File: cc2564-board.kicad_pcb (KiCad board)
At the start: 2 copper layers, 70 parts, among them J1 TYPE-C-31-M-12, J2 Conn_ARM_JTAG_SWD_10, J3 Conn_01x16, J4 Conn_01x16, J5 BOOT1, J6 BOOT0, J7 1909763-1, J8 Conn_01x04, SW1 SW_Push, U1 LD1117#33, U2 USBLC6-2P6, U3 LD1117#18, U4 STM32F103C8Tx, U5 TXB0104D, U6 TXB0104D, U7 CC2564CRVMR, Y1 ECS-80-18-30-JGN-TR, Y2 ECS-327MVATX-3-CN-TR, Y3 ECS-260-8-36CKM-TR

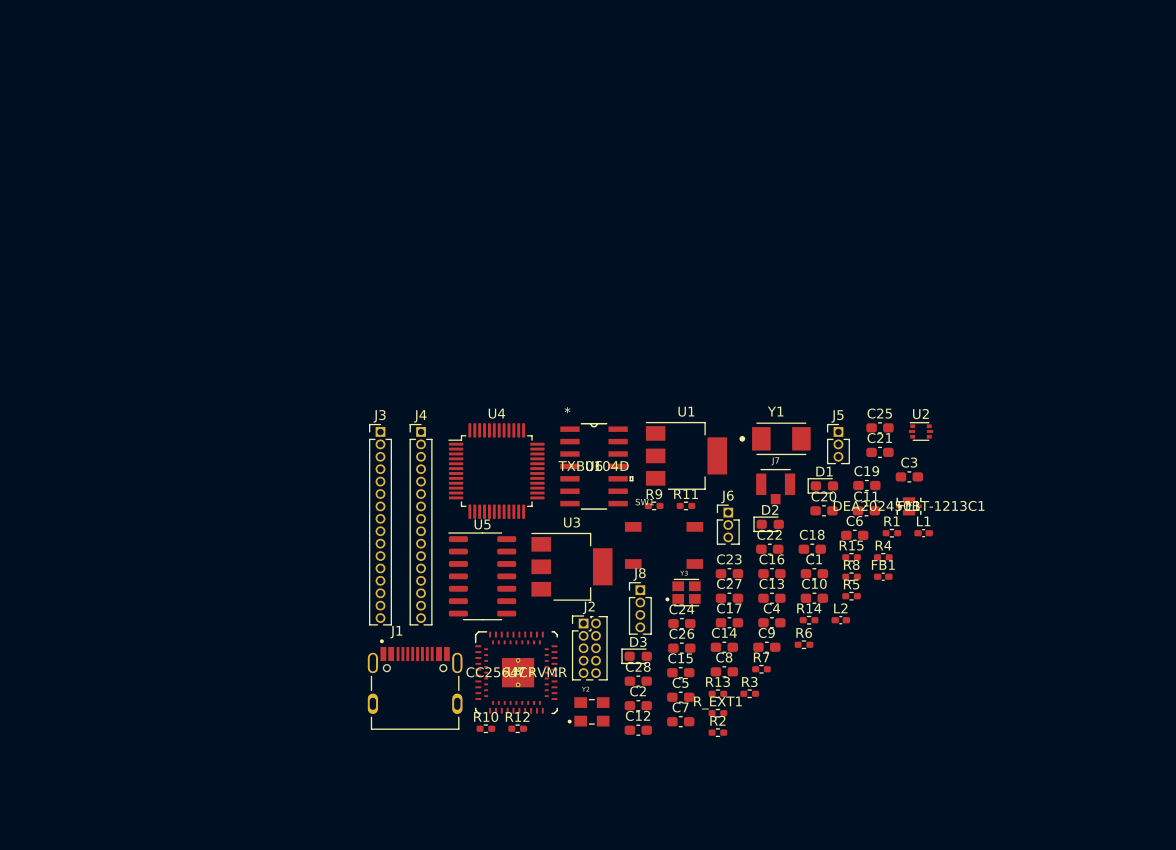
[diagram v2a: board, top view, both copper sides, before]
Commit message: One header for boot mode
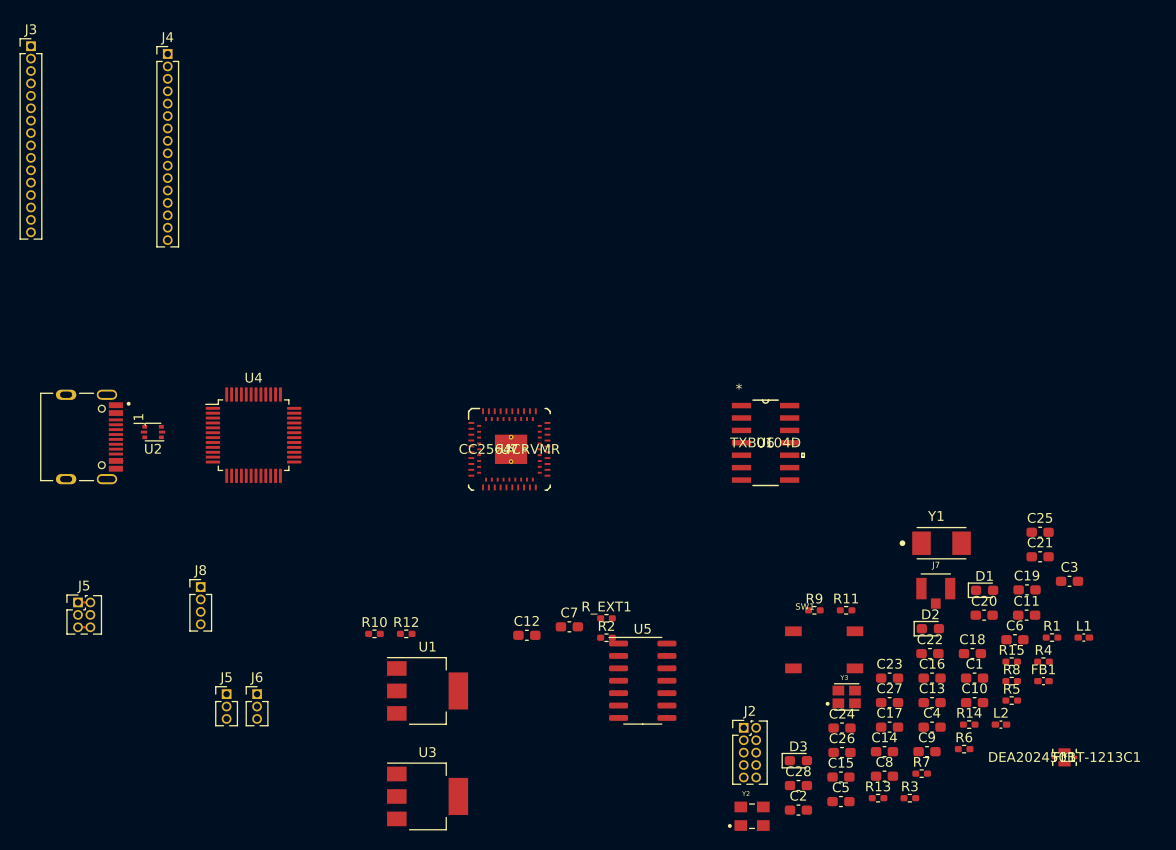
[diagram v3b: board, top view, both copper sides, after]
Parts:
- added J5: BOOT, Connector_PinHeader_1.27mm:PinHeader_2x03_P1.27mm_Vertical, F.Cu at (73.4, 81.7)
- moved U2 78.6 mm to (81.1, 64.3), turned to 180 degrees
- moved J5 68.1 mm to (88.6, 91.1)
- moved J3 53.3 mm to (68.6, 24.8)
- moved J6 51.7 mm to (91.7, 91.1)
- moved J4 46.6 mm to (82.6, 25.6)
- moved J8 45.0 mm to (86.0, 80.2)
- moved J1 45.0 mm to (72.2, 64.8), turned to 270 degrees
- moved U1 35.8 mm to (109.2, 90.8)
- moved FL1 30.2 mm to (174.4, 97.6)
- moved U3 27.8 mm to (109.2, 101.6)
- moved U4 25.2 mm to (91.4, 64.6)
- moved U7 22.9 mm to (117.6, 66.1)
- moved C11 19.6 mm to (170.5, 83.0)
- moved C13 19.6 mm to (160.8, 92.0)
- moved C15 19.6 mm to (151.5, 99.6)
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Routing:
- net VDD_3V3: track 0.00 -> 1.27 mm
- net GND: track 0.00 -> 1.27 mm
- net VCC_USB: track 0.00 -> 0.67 mm
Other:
- copper layers 2 -> 4

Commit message: Use meandered PIFA from TI app note AN043
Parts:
- added AE1: TI SWRA117D meandered IFA, RF_Antenna:Texas_SWRA117D_2.4GHz_Right, F.Cu at (213.6, 93.3)

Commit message: More footprint updates
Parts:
- C1, C10, C11, C12, C13, C14, C15, C16, C17, C18, C19, C2, C20, C21, C22, C23, C24, C25, C26, C27, C28, C3, C4, C5, C6, C7, C8, C9: footprint Capacitor_SMD:C_0603_1608Metric_Pad1.08x0.95mm_HandSolder -> Capacitor_SMD:C_0402_1005Metric_Pad0.74x0.62mm_HandSolder
- J5: value BOOT1 -> BOOT; footprint Connector_PinHeader_1.27mm:PinHeader_1x03_P1.27mm_Vertical -> Connector_PinHeader_1.27mm:PinHeader_2x03_P1.27mm_Vertical
- moved AE1 76.3 mm to (163.1, 36.1), turned to 270 degrees
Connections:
- J5 pad 2: BOOT1 -> VDD_3V3
- J5 pad 3: GND -> BOOT1

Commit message: Switch to nightly, initial board setup, not exactly sure what to git add...
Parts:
- removed the J5 at (88.6, 91.1)
- removed the J5 at (73.4, 81.7)
- removed J8: Conn_01x04, Connector_PinHeader_1.27mm:PinHeader_1x04_P1.27mm_Vertical
- removed Y3: ECS-260-8-36CKM-TR, cc2654-board-footprints:XTAL_ECS-160-10-36-JGN-TR
- added J5: BOOT, Connector_PinHeader_1.27mm:PinHeader_2x03_P1.27mm_Vertical, F.Cu at (134.2, 98.6)
- added R16: 10k, Resistor_SMD:R_0402_1005Metric_Pad0.72x0.64mm_HandSolder, F.Cu at (181.5, 101.7)
- added R17: 0, Resistor_SMD:R_0402_1005Metric_Pad0.72x0.64mm_HandSolder, F.Cu at (187.1, 97.8)
- C1, C11, C13, C3, C4, C5, C6, C8: value 100nF -> 0.1uF
- J6: value BOOT0 -> 1909763-1; footprint Connector_PinHeader_1.27mm:PinHeader_1x03_P1.27mm_Vertical -> cc2654-board-footprints:UFL-TE_1909763-1
- J7: value 1909763-1 -> Conn_01x04; footprint cc2654-board-footprints:UFL-TE_1909763-1 -> Connector_PinHeader_1.27mm:PinHeader_1x04_P1.27mm_Vertical
- R10: value 0 -> 10k
- R11: value 0 -> 1.5k
- R14: value 10k -> 0
- R4: value 90 -> 10k
- R5: value 55 -> 90
- R6: value 4 -> 55
- R7: value 10k -> 4
- R9: value 1.5k -> 10k
- moved J4 154.9 mm to (201.4, 125.0), turned to 180 degrees
- moved J1 140.9 mm to (190.6, 141.3), turned to 0 degrees
- moved J3 138.7 mm to (180.0, 107.4)
- moved U4 110.3 mm to (190.6, 112.8), turned to 90 degrees
- moved J6 108.3 mm to (199.9, 84.9), turned to -90 degrees
- moved U3 89.7 mm to (194.7, 128.8), turned to 90 degrees
- moved U1 85.9 mm to (186.2, 128.8), turned to 90 degrees
- moved U7 83.9 mm to (195.4, 97.3), turned to -90 degrees
- moved U2 75.1 mm to (153.5, 84.4), turned to 0 degrees
- moved Y1 53.5 mm to (190.5, 120.8), turned to 180 degrees
- moved AE1 53.0 mm to (191.0, 81.1), turned to 0 degrees
- moved L1 52.8 mm to (130.3, 111.2)
- moved R10 48.5 mm to (152.0, 89.6)
- moved C19 48.5 mm to (133.6, 111.8)
- moved SW1 46.4 mm to (110.1, 110.6)
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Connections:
- net Net-(J1-PadA8) renamed no_connect_77
- net Net-(J1-PadB8) renamed no_connect_78
- net Net-(J2-Pad8) renamed no_connect_79
- net Net-(U4-Pad2) renamed no_connect_80
- net Net-(U4-Pad3) renamed no_connect_81
- net Net-(U4-Pad4) renamed no_connect_82
- net Net-(U5-Pad10) renamed no_connect_83
- net Net-(U5-Pad11) renamed no_connect_84
- net Net-(U5-Pad12) renamed no_connect_85
- net Net-(U5-Pad3) renamed no_connect_86
- net Net-(U5-Pad4) renamed no_connect_87
- net Net-(U5-Pad5) renamed no_connect_88
- net Net-(U7-PadA1) renamed no_connect_89
- net Net-(U7-PadA12) renamed no_connect_90
- net Net-(U7-PadA13) renamed no_connect_91
- net Net-(U7-PadA14) renamed no_connect_92
- net Net-(U7-PadA15) renamed no_connect_93
- net Net-(U7-PadA16) renamed no_connect_94
- net Net-(U7-PadA18) renamed no_connect_95
- net Net-(U7-PadA19) renamed no_connect_96
- net Net-(U7-PadA20) renamed no_connect_97
- net Net-(U7-PadA21) renamed no_connect_98
- net Net-(U7-PadA22) renamed no_connect_99
- net Net-(U7-PadA23) renamed no_connect_100
- net Net-(U7-PadA27) renamed no_connect_101
- net Net-(U7-PadA30) renamed no_connect_102
- net Net-(U7-PadA31) renamed no_connect_103
- net Net-(U7-PadA35) renamed no_connect_104
- net Net-(U7-PadA36) renamed no_connect_105
- net Net-(U7-PadA37) renamed no_connect_106
- net Net-(U7-PadA39) renamed no_connect_107
- net Net-(U7-PadA40) renamed no_connect_108
- net Net-(U7-PadA7) renamed no_connect_109
- net Net-(U7-PadA8) renamed no_connect_110
- net Net-(U7-PadB1) renamed no_connect_111
- net Net-(U7-PadB10) renamed no_connect_112
- net Net-(U7-PadB12) renamed no_connect_113
- net Net-(U7-PadB13) renamed no_connect_114
- net Net-(U7-PadB14) renamed no_connect_115
- net Net-(U7-PadB16) renamed no_connect_116
- net Net-(U7-PadB17) renamed no_connect_117
- net Net-(U7-PadB20) renamed no_connect_118
- net Net-(U7-PadB23) renamed no_connect_119
- net Net-(U7-PadB28) renamed no_connect_120
- net Net-(U7-PadB29) renamed no_connect_121
- net Net-(U7-PadB30) renamed no_connect_122
- net Net-(U7-PadB31) renamed no_connect_123
- net Net-(U7-PadB32) renamed no_connect_124
- net Net-(U7-PadB33) renamed no_connect_125
- net Net-(U7-PadB34) renamed no_connect_126
- J2 pad 7: Net-(J2-Pad7) -> (no net)
- J6 pad 1: VDD_3V3 -> Net-(J6-Pad1)
- J6 pad 2: BOOT0 -> GND
- J7 pad 1: Net-(J7-Pad1) -> NSHUTDOWN_1V8
- J7 pad 2: GND -> BT_TX_DBG
- R10 pad 2: USB_D- -> BOOT1
- R11 pad 1: USB_D+ -> VDD_3V3
- R11 pad 2: Net-(R11-Pad2) -> USB_D+
- R12 pad 1: Net-(AE1-Pad1) -> Net-(R12-Pad1)
- R12 pad 2: Net-(C21-Pad1) -> USB_D-
- R13 pad 1: Net-(J7-Pad1) -> USB_D+
- R13 pad 2: Net-(C21-Pad1) -> Net-(R13-Pad2)
- R14 pad 1: VDD_1V8_32K -> Net-(AE1-Pad1)
- R14 pad 2: Net-(R14-Pad2) -> Net-(C21-Pad1)
- R15 pad 1: BT_SLOW_CLK -> Net-(J6-Pad1)
- R15 pad 2: Net-(R15-Pad2) -> Net-(C21-Pad1)
- R4 pad 1: VCC_USB -> Net-(R4-Pad1)
- R4 pad 2: Net-(D1-Pad2) -> BOOT0
- R5 pad 1: VDD_3V3 -> VCC_USB
- R5 pad 2: Net-(D2-Pad2) -> Net-(D1-Pad2)
- R6 pad 1: VDD_1V8 -> VDD_3V3
- R6 pad 2: Net-(D3-Pad2) -> Net-(D2-Pad2)
- R7 pad 1: VDD_3V3 -> VDD_1V8
- R7 pad 2: Net-(R7-Pad2) -> Net-(D3-Pad2)
- R9 pad 2: USB_D+ -> Net-(R9-Pad2)
- U4 pad 20: BOOT1 -> Net-(R10-Pad1)
- U4 pad 32: Net-(R10-Pad1) -> Net-(R12-Pad1)
- U4 pad 33: Net-(R11-Pad2) -> Net-(R13-Pad2)
- U4 pad 44: BOOT0 -> Net-(R4-Pad1)
- U5 pad 6: Net-(U5-Pad6) -> (no net)
- U5 pad 8: Net-(R7-Pad2) -> Net-(R8-Pad2)
- U5 pad 9: Net-(U5-Pad9) -> (no net)
- U6 pad 6: Net-(U6-Pad6) -> (no net)
- U6 pad 8: Net-(R8-Pad2) -> Net-(R9-Pad2)
- U6 pad 9: Net-(U6-Pad9) -> (no net)
- Y2 pad 1: Net-(R14-Pad2) -> Net-(R16-Pad2)
- Y2 pad 3: Net-(R15-Pad2) -> Net-(R17-Pad2)
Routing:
- net Net-(C22-Pad2): track 0.00 -> 3.68 mm
- net VDD_3V3: track 1.27 -> 0.00 mm
- net GND: track 1.27 -> 0.00 mm
- net VCC_USB: track 0.67 -> 0.00 mm
- added copper zone on In1.Cu, net GND
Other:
- board outline added: 25.9 x 67.9 mm
- net class Default removed

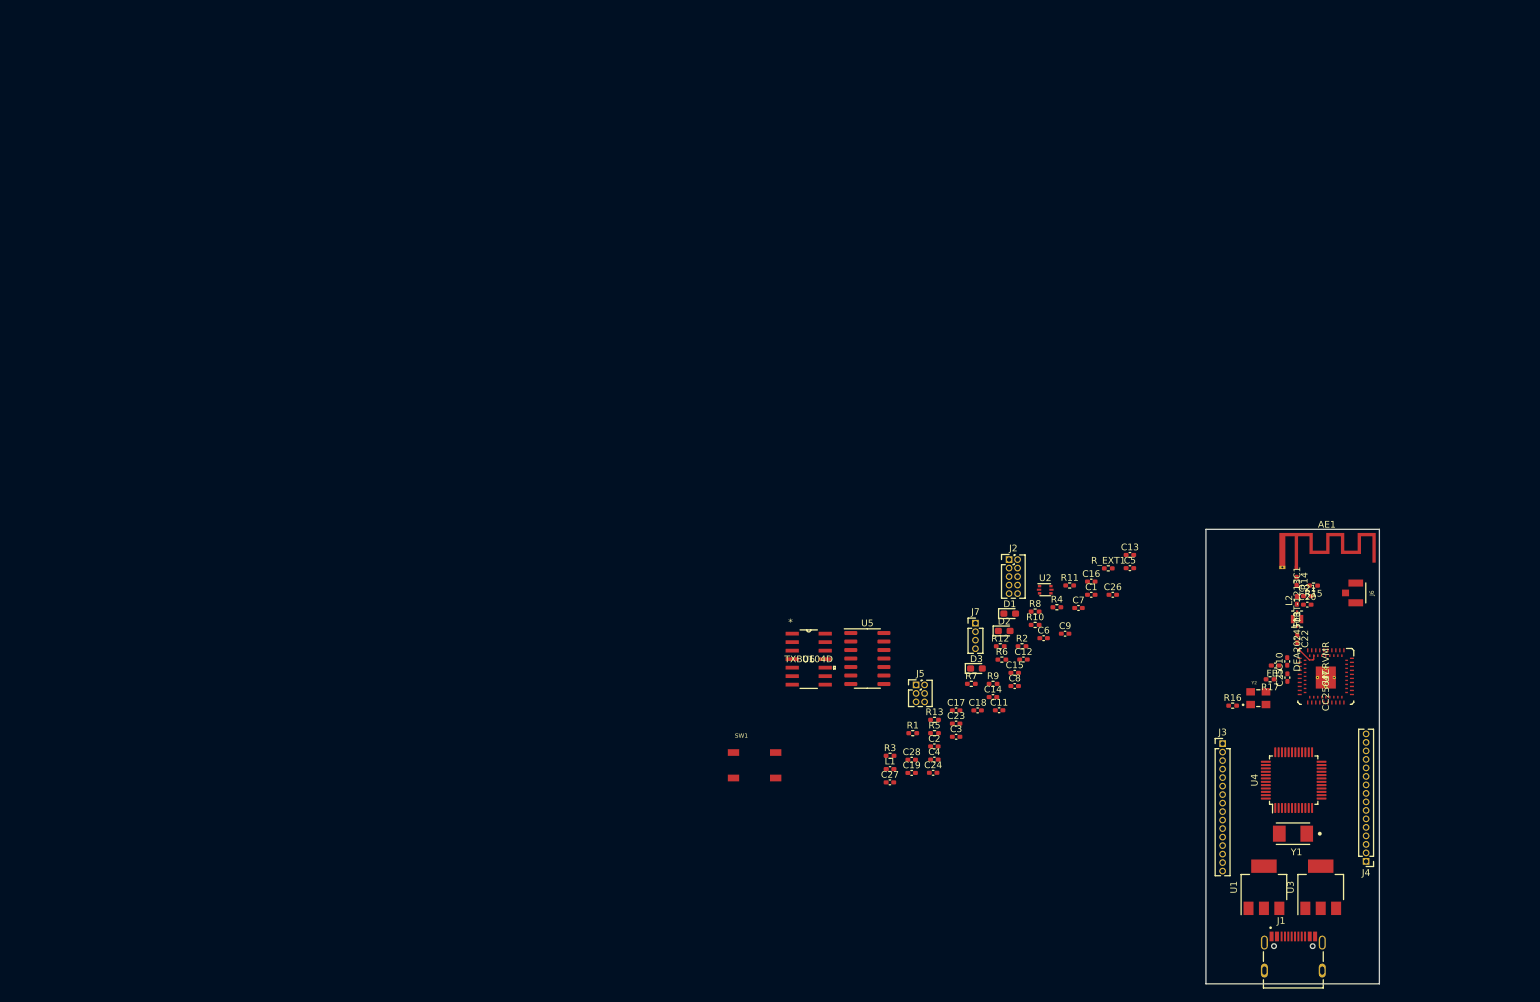
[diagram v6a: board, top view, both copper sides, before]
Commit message: Swap in TLV711 series 3v3/1v8 dual output LDO
Thanks @noahp for inspiration
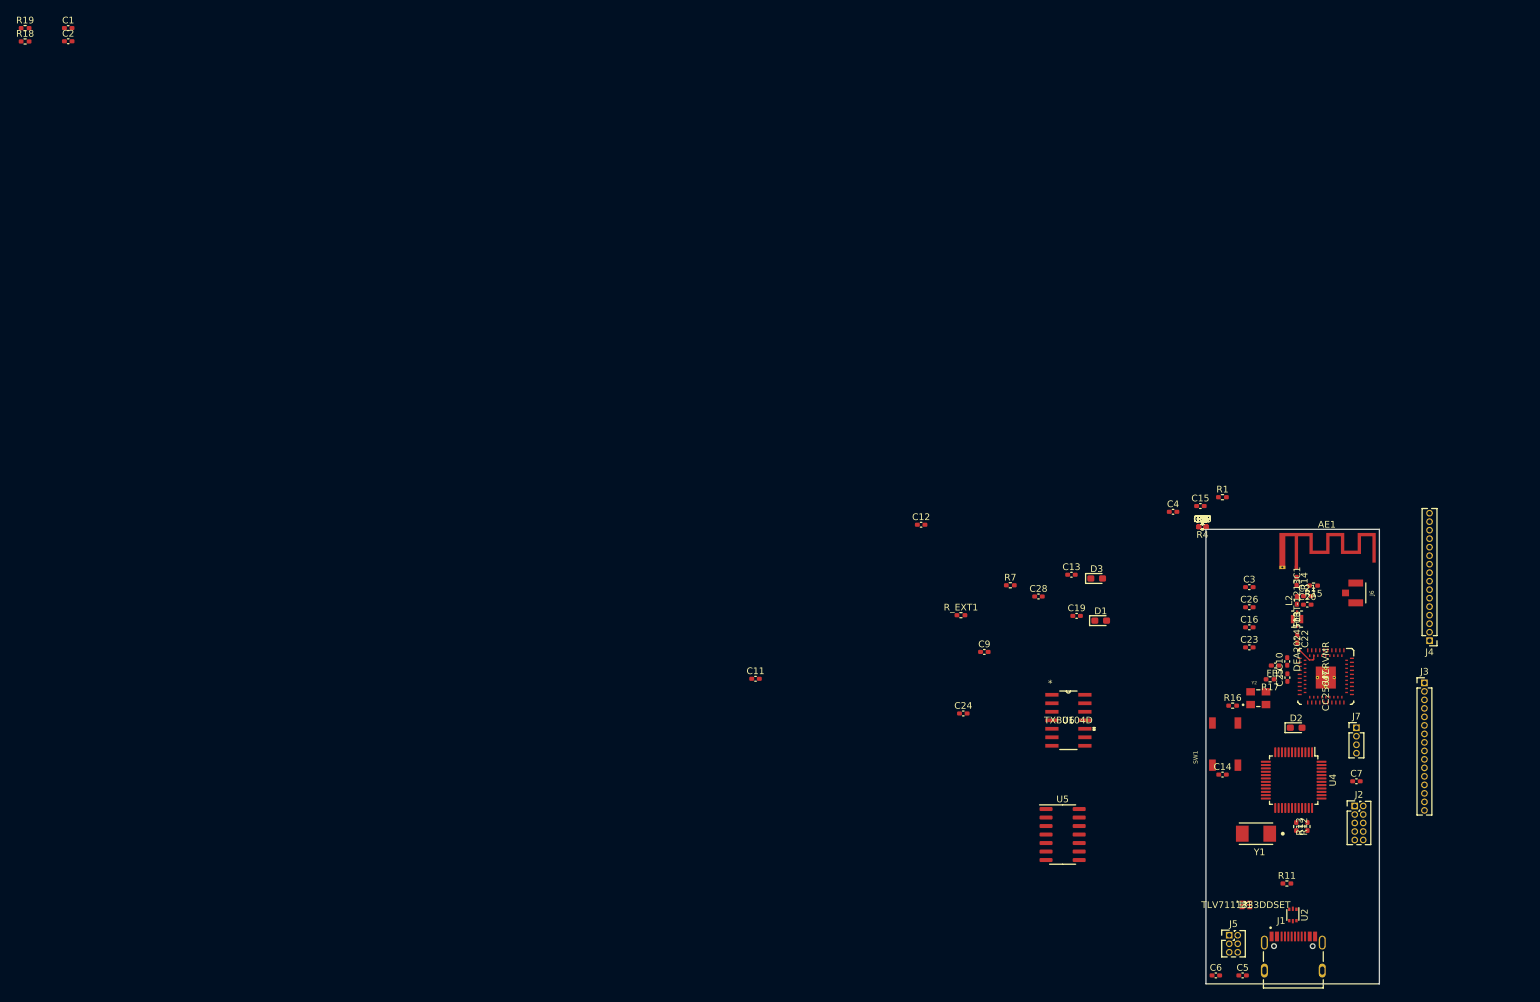
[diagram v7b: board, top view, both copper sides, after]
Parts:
- removed U3: LD1117#18, Package_TO_SOT_SMD:SOT-223-3_TabPin2
- added R18: 10k, Resistor_SMD:R_0402_1005Metric_Pad0.72x0.64mm_HandSolder, F.Cu at (1.12, 2.48)
- added R19: 10k, Resistor_SMD:R_0402_1005Metric_Pad0.72x0.64mm_HandSolder, F.Cu at (1.12, 0.49)
- C12, C2: value 10uF -> 0.1uF
- U1: value LD1117#33 -> TLV7111833DDSET; footprint Package_TO_SOT_SMD:SOT-223-3_TabPin2 -> cc2654-board-footprints:TLV7111833DDSET
- moved C1 174.7 mm to (7.57, 0.48)
- moved C2 166.8 mm to (7.57, 2.46)
- moved SW1 70.4 mm to (180.4, 107.4), turned to 90 degrees
- moved J2 63.4 mm to (199.7, 116.7)
- moved C5 63.1 mm to (183.0, 142.0)
- moved U2 61.1 mm to (190.5, 133.0), turned to -90 degrees
- moved C27 60.3 mm to (177.0, 75.0)
- moved J5 59.9 mm to (181.0, 136.0)
- moved L1 59.1 mm to (177.0, 75.0)
- moved J7 59.0 mm to (200.0, 105.0)
- moved R1 58.2 mm to (180.0, 70.6)
- moved R13 57.9 mm to (192.7, 119.8), turned to 90 degrees
- moved R3 57.9 mm to (177.0, 75.0)
- moved C6 56.6 mm to (179.0, 142.0)
- moved R11 55.1 mm to (189.6, 128.3)
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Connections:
- C1 pad 2: VCC_USB -> VDD_1V8
- C12 pad 1: GND -> Net-(C12-Pad1)
- C12 pad 2: VDD_1V8 -> Net-(C12-Pad2)
- J1 pad A8: no_connect_77 -> no_connect_81
- J1 pad B8: no_connect_78 -> no_connect_82
- J2 pad 8: no_connect_79 -> no_connect_83
- U1 pad 1: GND -> Net-(R19-Pad1)
- U1 pad 2: VDD_3V3 -> VCC_USB
- U1 pad 3: VCC_USB -> Net-(R18-Pad1)
- U4 pad 2: no_connect_80 -> no_connect_84
- U4 pad 3: no_connect_81 -> no_connect_85
- U4 pad 4: no_connect_82 -> no_connect_86
- U5 pad 10: no_connect_83 -> no_connect_87
- U5 pad 11: no_connect_84 -> no_connect_88
- U5 pad 12: no_connect_85 -> no_connect_89
- U5 pad 3: no_connect_86 -> no_connect_90
- U5 pad 4: no_connect_87 -> no_connect_91
- U5 pad 5: no_connect_88 -> no_connect_92
- U7 pad A1: no_connect_89 -> no_connect_93
- U7 pad A12: no_connect_90 -> no_connect_94
- U7 pad A13: no_connect_91 -> no_connect_95
- U7 pad A14: no_connect_92 -> no_connect_96
- U7 pad A15: no_connect_93 -> no_connect_97
- U7 pad A16: no_connect_94 -> no_connect_98
- U7 pad A18: no_connect_95 -> no_connect_99
- U7 pad A19: no_connect_96 -> no_connect_100
- U7 pad A20: no_connect_97 -> no_connect_101
- U7 pad A21: no_connect_98 -> no_connect_102
- U7 pad A22: no_connect_99 -> no_connect_103
- U7 pad A23: no_connect_100 -> no_connect_104
- U7 pad A27: no_connect_101 -> no_connect_105
- U7 pad A30: no_connect_102 -> no_connect_106
- U7 pad A31: no_connect_103 -> no_connect_107
- U7 pad A35: no_connect_104 -> no_connect_108
- U7 pad A36: no_connect_105 -> no_connect_109
- U7 pad A37: no_connect_106 -> no_connect_110
- U7 pad A39: no_connect_107 -> no_connect_111
- U7 pad A40: no_connect_108 -> no_connect_112
- U7 pad A7: no_connect_109 -> no_connect_113
- U7 pad A8: no_connect_110 -> no_connect_114
- U7 pad B1: no_connect_111 -> no_connect_115
- U7 pad B10: no_connect_112 -> no_connect_116
- U7 pad B12: no_connect_113 -> no_connect_117
- U7 pad B13: no_connect_114 -> no_connect_118
- U7 pad B14: no_connect_115 -> no_connect_119
- U7 pad B16: no_connect_116 -> no_connect_120
- U7 pad B17: no_connect_117 -> no_connect_121
- U7 pad B20: no_connect_118 -> no_connect_122
- U7 pad B23: no_connect_119 -> no_connect_123
- U7 pad B28: no_connect_120 -> no_connect_124
- U7 pad B29: no_connect_121 -> no_connect_125
- U7 pad B30: no_connect_122 -> no_connect_126
- U7 pad B31: no_connect_123 -> no_connect_127
- U7 pad B32: no_connect_124 -> no_connect_128
- U7 pad B33: no_connect_125 -> no_connect_129
- U7 pad B34: no_connect_126 -> no_connect_130

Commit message: Temp top ground fill, generally make a mess
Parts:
- moved R19 185.7 mm to (138.5, 125.4)
- moved R18 182.1 mm to (142.0, 117.8)
- moved C1 177.4 mm to (145.7, 111.8)
- moved C2 164.8 mm to (124.0, 119.1)
- moved R5 59.5 mm to (186.1, 133.8)
- moved D1 49.3 mm to (185.8, 132.1)
- moved R9 36.9 mm to (162.6, 109.0)
- moved L1 24.9 mm to (167.2, 97.8)
- moved R8 11.3 mm to (167.9, 81.8)
- moved C17 8.65 mm to (185.1, 78.0)
- moved C8 7.70 mm to (184.1, 78.0)
- moved C18 6.76 mm to (183.1, 78.0)
- moved C27 5.86 mm to (182.0, 78.0)
- moved U1 5.10 mm to (184.4, 126.4)
- moved R4 5.01 mm to (181.0, 78.0)
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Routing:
- net Net-(D1-Pad2): track 0.00 -> 3.50 mm
- net USB_CONN_D-: track 0.00 -> 2.33 mm
- net USB_CONN_D+: track 0.00 -> 2.29 mm
- net VCC_USB: track 0.00 -> 1.97 mm, vias 0 -> 2
- added copper zone on B.Cu, net GND
- added copper zone on F.Cu, net GND
